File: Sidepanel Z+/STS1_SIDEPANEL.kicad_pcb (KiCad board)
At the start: 4 copper layers, 82.8 x 100 mm, 30 parts, among them IC1 TMP112AQDRLRQ1, J1 Conn_01x08, U1 GUVA-C32SM, U11 INA180A4

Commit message: Changed the values of the VCTRL resistors.
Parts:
- R61: value 1M -> 3k
- R71: value 330k -> 1k
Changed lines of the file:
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@@
 			)
 		)
+		(sheetname "Root")
+		(sheetfile "STS1_SIDEPANEL.kicad_sch")
 		(attr exclude_from_bom)
 		(fp_line
@@
 		(fp_arc
 			(start 40.84 -46.43)
-			(mid 41.190544 -46.303303)
+			(mid 41.190522 -46.303293)
 			(end 41.4 -45.995)
 			(stroke
@@
 			)
 		)
-		(property "Value" "330k"
+		(property "Value" "1k"
 			(at 0 -1.43 90)
 			(layer "B.Fab")
@@
 			)
 		)
-		(property "Value" "1M"
+		(property "Value" "3k"
 			(at 0 -1.43 90)
 			(layer "B.Fab")
@@
 		)
 		(property ki_fp_filters "Connector*:*_1x??_*")
-		(sheetname "Stammblatt")
+		(sheetname "Root")
 		(sheetfile "STS1_SIDEPANEL.kicad_sch")
 		(attr smd allow_soldermask_bridges)
@@
 			)
 		)
-		(sheetname "Stammblatt")
+		(sheetname "Root")
 		(sheetfile "STS1_SIDEPANEL.kicad_sch")
 		(attr smd)
@@
 			)
 		)
-		(sheetname "Stammblatt")
+		(sheetname "Root")
 		(sheetfile "STS1_SIDEPANEL.kicad_sch")
 		(attr smd)
@@
 		)
 		(property ki_fp_filters "*NTC* *Thermistor* PIN?ARRAY* bornier* *Terminal?Block* R_*")
-		(sheetname "Stammblatt")
+		(sheetname "Root")
 		(sheetfile "STS1_SIDEPANEL.kicad_sch")
 		(attr smd)
@@
 			)
 		)
-		(sheetname "Stammblatt")
+		(sheetname "Root")
 		(sheetfile "STS1_SIDEPANEL.kicad_sch")
 		(attr smd)

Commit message: Updated according to the review from Dhruva.
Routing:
- net /MPPT1: track 93.3 -> 96.8 mm
- net /SolarMPPT/CUR1_OUT: track 20.3 -> 23.0 mm
- net GND: track 17.8 -> 19.8 mm
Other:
- outline, holes or cut-outs redrawn
- board text added: "Z+ V3.0"
- board text removed: "Z+ V2.5"

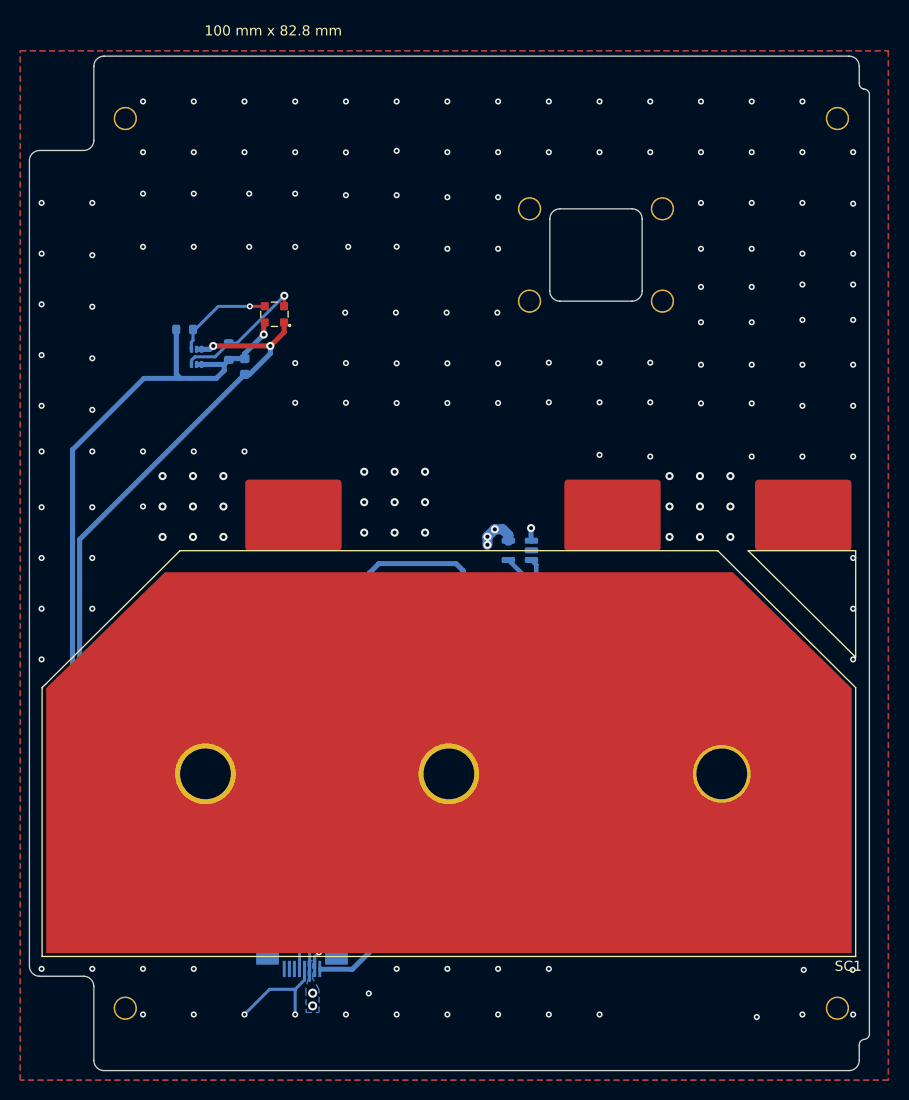
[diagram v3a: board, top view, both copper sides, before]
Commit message: changed all vias from blind to trough and removed the unused pins of the uci connector
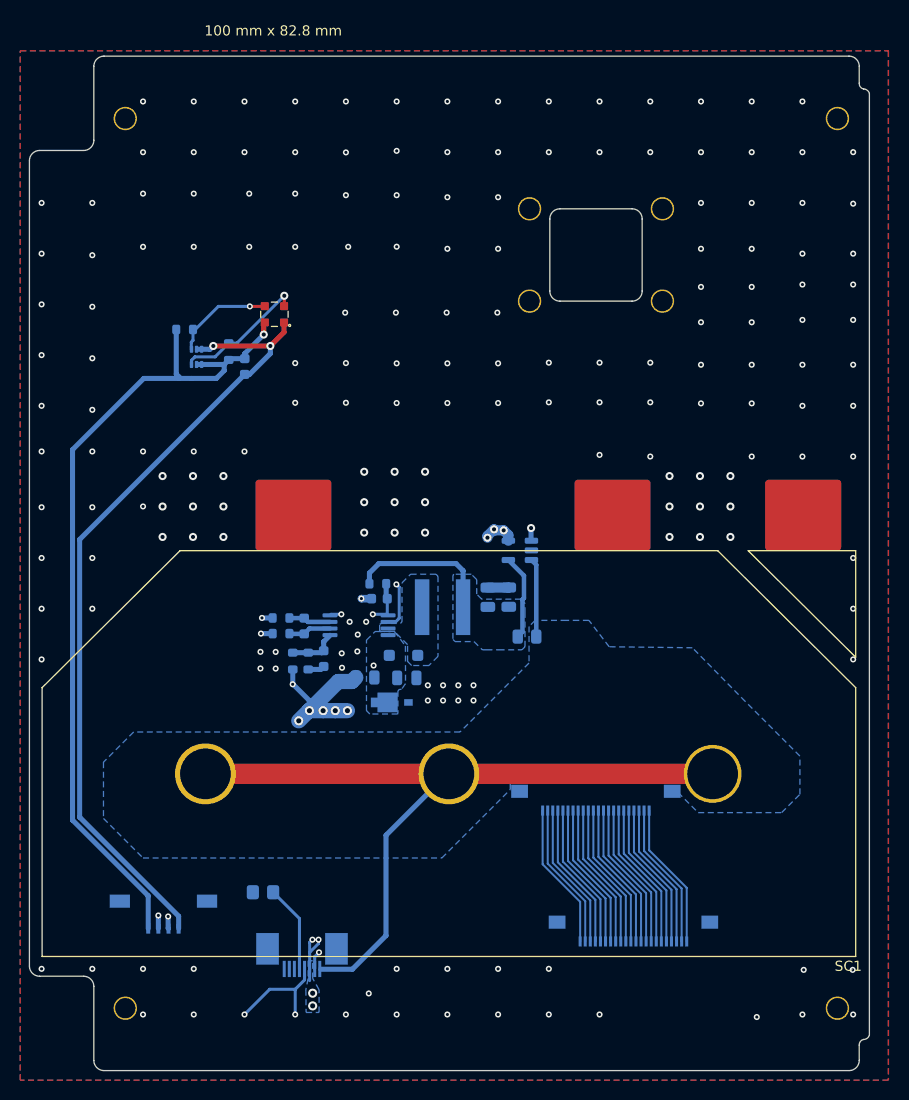
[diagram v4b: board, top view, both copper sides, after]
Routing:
- net /SC1_V+: track 42.3 -> 84.0 mm

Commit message: chaned the connectors for the cameras from buttom to top contact
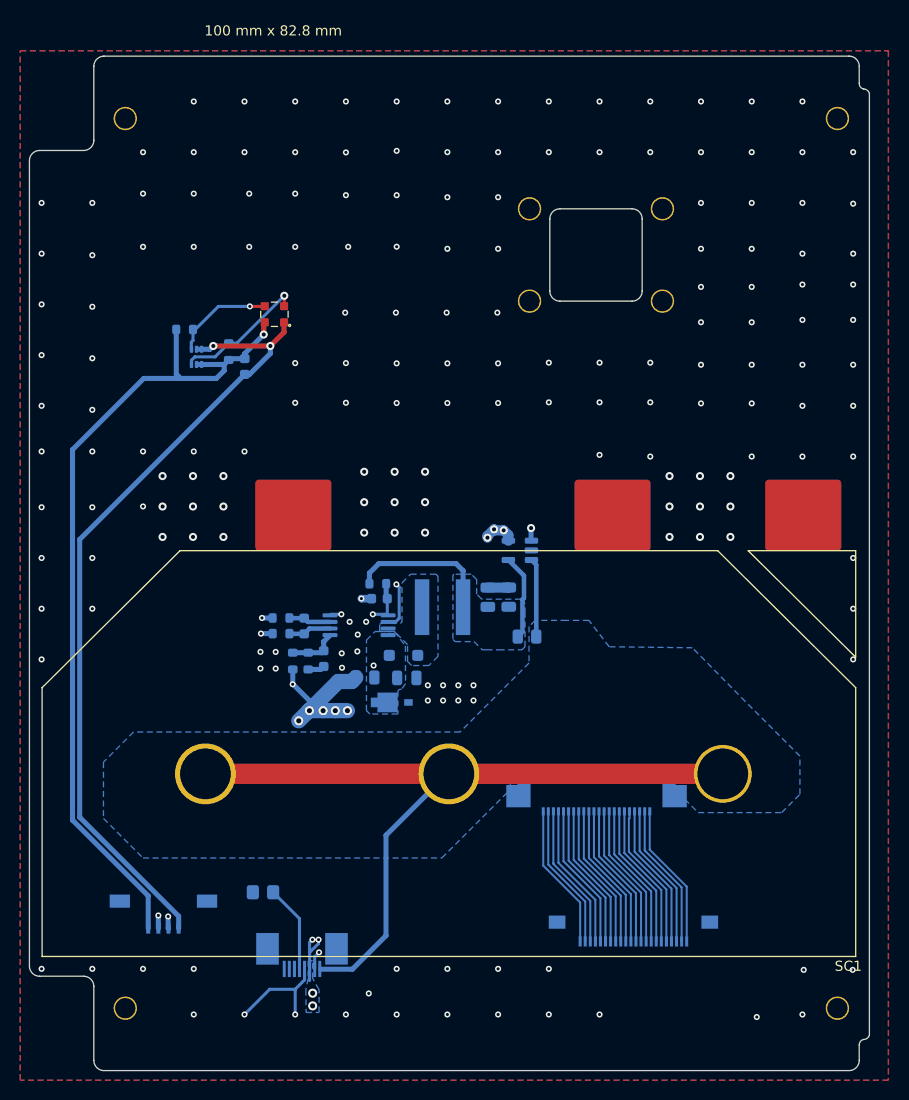
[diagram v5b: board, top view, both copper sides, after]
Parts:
- cam2: value 54548-2271 -> 52435-2271; footprint STS_connector:545482271 -> STS_connector:524352271
- moved cam2 0.43 mm to (139.7, 111.9)
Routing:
- net GND: vias 191 -> 188

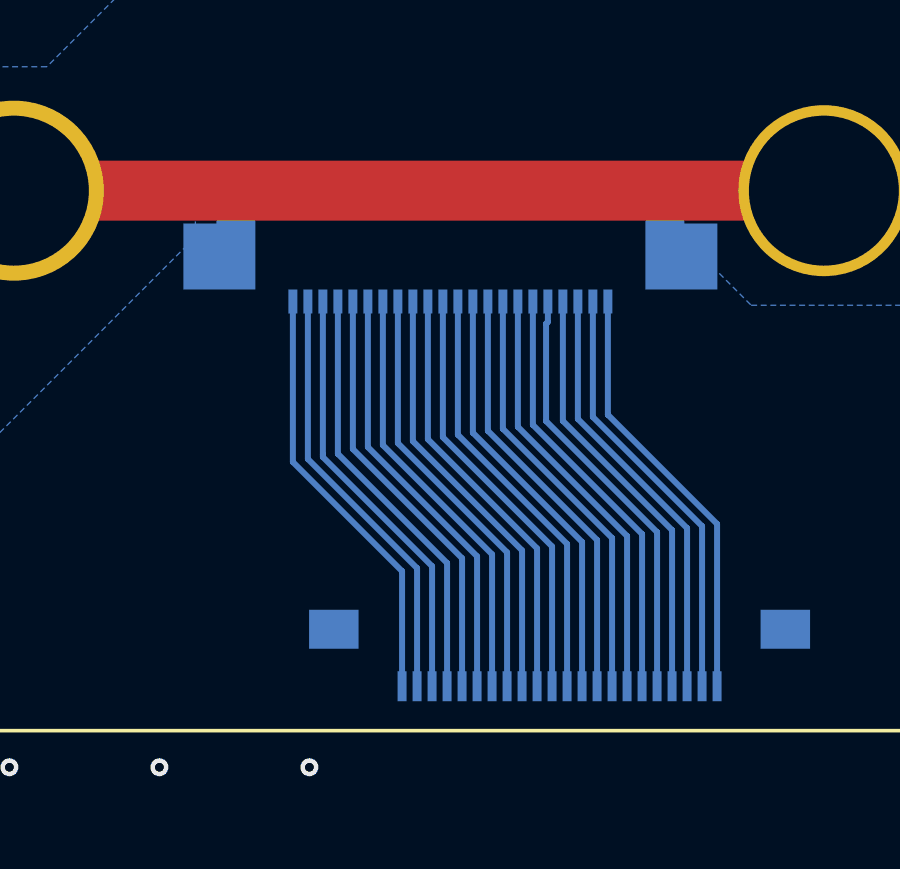
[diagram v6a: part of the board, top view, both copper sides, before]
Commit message: moved the camera connectors to be sure that the cable can be inserted
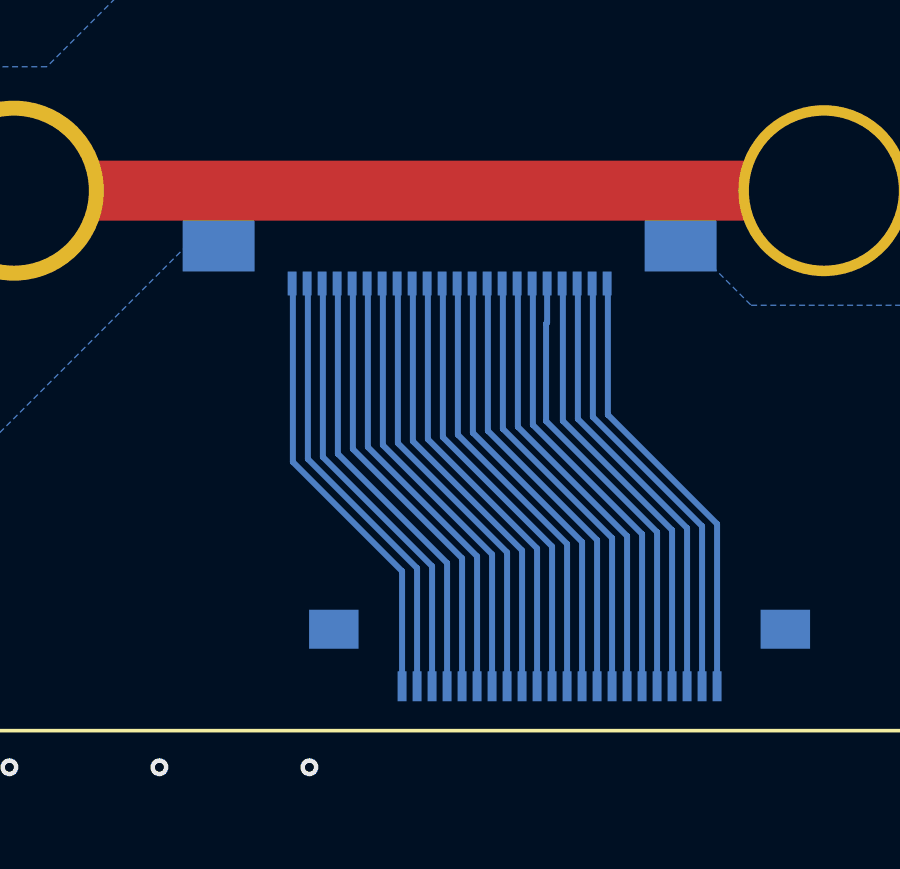
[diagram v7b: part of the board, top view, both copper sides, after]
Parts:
- moved cam2 0.60 mm to (139.7, 111.3)
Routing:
- net Net-(cam2-Pad4): track 14.3 -> 14.9 mm
- net Net-(cam2-Pad20): track 14.3 -> 14.9 mm
- net Net-(cam2-Pad9): track 14.3 -> 14.9 mm
- net Net-(cam2-Pad8): track 14.3 -> 14.9 mm
- net Net-(cam2-Pad7): track 14.3 -> 14.9 mm
- net Net-(cam2-Pad6): track 14.3 -> 14.9 mm
- net Net-(cam2-Pad5): track 14.3 -> 14.9 mm
- net Net-(cam2-Pad3): track 14.3 -> 14.9 mm
- net Net-(cam2-Pad22): track 14.3 -> 14.9 mm
- net Net-(cam2-Pad21): track 14.3 -> 14.9 mm
- net Net-(cam2-Pad2): track 14.3 -> 14.9 mm
- net Net-(cam2-Pad19): track 14.3 -> 14.9 mm
- net Net-(cam2-Pad17): track 14.3 -> 14.9 mm
- net Net-(cam2-Pad16): track 14.3 -> 14.9 mm
- net Net-(cam2-Pad15): track 14.3 -> 14.9 mm
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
